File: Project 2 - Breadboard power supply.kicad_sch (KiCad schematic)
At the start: 17 parts, among them J1 Conn_01x02_Pin, J2 Conn_01x02_Pin, J3 Conn_01x03_Pin, J4 Conn_01x03_Pin, J5 Screw_Terminal_01x02, J6 Barrel_Jack_Switch, J7 Screw_Terminal_01x02, U1 LM7805_TO220, U2 LM317_TO-220

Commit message: make measurements
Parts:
- removed S1: EG1218, EG1218:SW_EG1218, symbol EG1218:EG1218
- added SW1: EG1218, EG1218:SW_1218_EWI, symbol EG1218:EG1218
- D1: Purpose (none) -> Power input indicator
- J1, J2: Purpose (none) -> Output to breadboard
- J3: Purpose (none) -> Output voltage selector 1
- J4: Purpose (none) -> Output voltage selector 2
- J5, J7: Purpose (none) -> Output to jumper wires
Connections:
- net 12V: now reaches C1.1
- net 12V: now also R2.2, U1.1 (VI), U2.3 (VI), SW1.2
- net GND: now reaches C1.2
- net GND: now also C2.2, C3.2, D1.1 (K), J1.1 (Pin_1), J2.1 (Pin_1), J5.1 (Pin_1), J6.2, J6.3, J7.1 (Pin_1), R3.1, U1.2 (GND)
- net PWR_OUTPUT: now reaches J1.2 (Pin_2)
- net PWR_OUTPUT: now also J2.2 (Pin_2), J3.2 (Pin_2), J4.2 (Pin_2), J5.2 (Pin_2), J7.2 (Pin_2)
- net 3.3V: now reaches J3.1 (Pin_1)
- net 3.3V: now also C3.1, J4.1 (Pin_1), R1.2, U2.2 (VO)
- net 5V: now reaches J3.3 (Pin_3)
- net 5V: now also C2.1, J4.3 (Pin_3), U1.3 (VO)
- net at D1.2 (A): now also R2.1
- net at R1.1: now also R3.2, U2.1 (ADJ)
- net PWR_INPUT: now reaches J6.1
- net PWR_INPUT: now also SW1.1
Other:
- note added: "3.3V Circuit"
- note added: "Did not flip the screw terminal vertically"
- note added: "Did not flip the screw terminal vertically intentionally"
- note added: "Input and 5V circuit"
- note added: "Output and switches"
- note added: "The capacitor acts like a filter which smoothens the input signal"
- moved on the sheet: C1, C2, C3, D1, J1, J2, J3, J4, J5, J6, J7, R1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

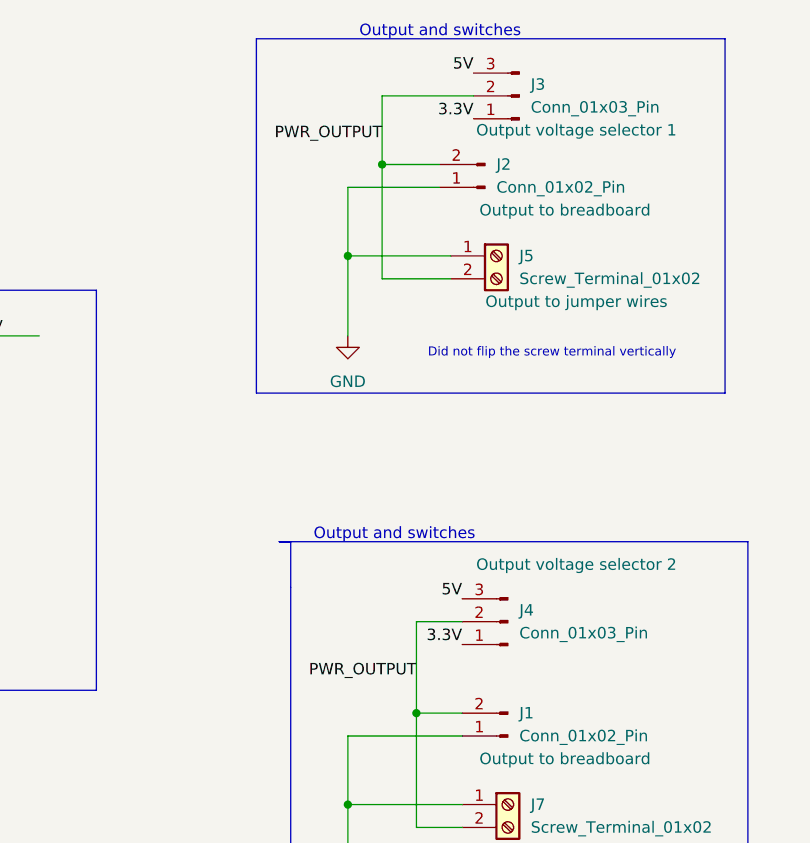
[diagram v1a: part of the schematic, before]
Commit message: fix power_output net label
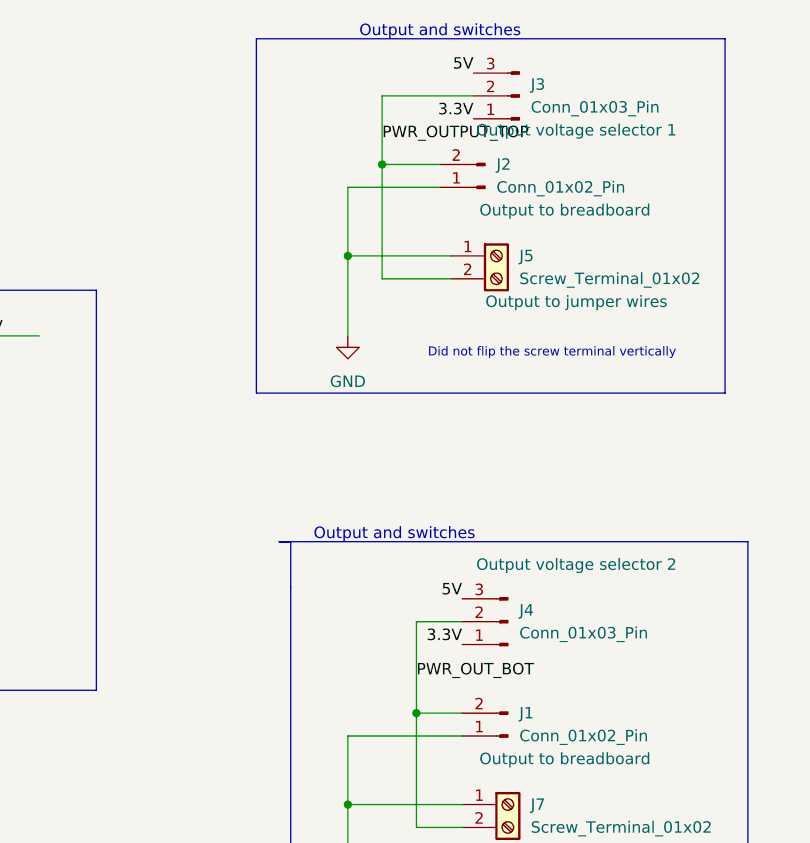
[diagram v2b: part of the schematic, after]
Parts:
- J3, J4: footprint Connector_PinHeader_2.54mm:PinHeader_1x02_P2.54mm_Vertical -> Connector_PinHeader_2.54mm:PinHeader_1x03_P2.54mm_Vertical
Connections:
- net PWR_OUTPUT renamed PWR_OUTPUT_TOP
- net PWR_OUTPUT_TOP: no longer J1.2 (Pin_2), J4.2 (Pin_2), J7.2 (Pin_2)
- new net PWR_OUT_BOT: J1.2 (Pin_2), J4.2 (Pin_2), J7.2 (Pin_2)
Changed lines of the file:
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@@
     (effects (font (size 1.27 1.27)) (justify left bottom))
   )
-  (label "PWR_OUTPUT" (at 187.96 86.36 180) (fields_autoplaced)
-    (effects (font (size 1.27 1.27)) (justify right bottom))
+  (label "PWR_OUT_BOT" (at 187.96 86.36 0) (fields_autoplaced)
+    (effects (font (size 1.27 1.27)) (justify left bottom))
   )
   (label "5V" (at 193.04 77.47 180) (fields_autoplaced)
     (effects (font (size 1.27 1.27)) (justify right bottom))
   )
-  (label "PWR_OUTPUT" (at 184.15 26.67 180) (fields_autoplaced)
-    (effects (font (size 1.27 1.27)) (justify right bottom))
+  (label "PWR_OUTPUT_TOP" (at 184.15 26.67 0) (fields_autoplaced)
+    (effects (font (size 1.27 1.27)) (justify left bottom))
   )
   (label "3.3V" (at 194.31 24.13 180) (fields_autoplaced)
@@
       (effects (font (size 1.27 1.27)) (justify right))
     )
-    (property "Footprint" "Connector_PinHeader_2.54mm:PinHeader_1x02_P2.54mm_Vertical" (at 199.39 21.59 0)
+    (property "Footprint" "Connector_PinHeader_2.54mm:PinHeader_1x03_P2.54mm_Vertical" (at 199.39 21.59 0)
       (effects (font (size 1.27 1.27)) hide)
     )
@@
       (effects (font (size 1.27 1.27)) (justify right))
     )
-    (property "Footprint" "Connector_PinHeader_2.54mm:PinHeader_1x02_P2.54mm_Vertical" (at 198.12 80.01 0)
-      (effects (font (size 1.27 1.27)) hide)
-    )
+    (property "Footprint" "Connector_PinHeader_2.54mm:PinHeader_1x03_P2.54mm_Vertical" (at 198.12 80.01 0)
+      (effects (font (size 1.27 1.27)) hide)
+    )
